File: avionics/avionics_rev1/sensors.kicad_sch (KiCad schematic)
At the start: 11 parts, among them U10 LSM6DSV32XTR, U8 LPS22DFTR, U9 ADXL375BCCZ-RL7

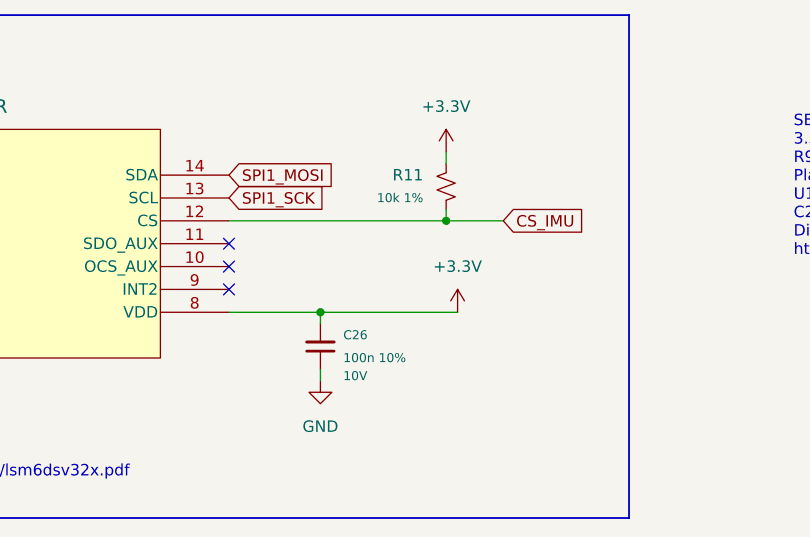
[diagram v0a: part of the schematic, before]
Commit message: cleaned up schematics after codex work
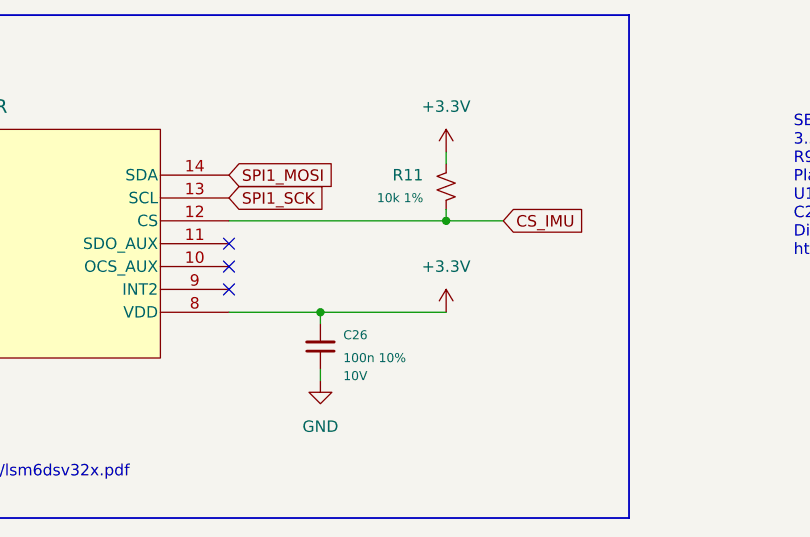
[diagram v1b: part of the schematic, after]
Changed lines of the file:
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@@
+	)
+	(junction
+		(at 124.46 119.38)
+		(diameter 0)
+		(color 0 0 0 0)
 	)
 	(junction
@@
 		(color 0 0 0 0)
 	)
-	(junction
-		(at 124.46 119.38)
-		(diameter 0)
-		(color 0 0 0 0)
-	)
 	(no_connect
 		(at 114.3 114.3)
@@
 	(wire
 		(pts
-			(xy 124.46 119.38) (xy 139.7 119.38)
+			(xy 124.46 119.38) (xy 138.43 119.38)
 		)
 		(stroke
@@
 	(symbol
 		(lib_id "power:+3.3V")
-		(at 139.7 119.38 0)
+		(at 138.43 119.38 0)
 		(unit 1)
 		(body_style 1)
@@
 		(fields_autoplaced yes)
 		(property "Reference" "#PWR047"
-			(at 139.7 123.19 0)
+			(at 138.43 123.19 0)
 			(hide yes)
 			(show_name no)
@@
 		)
 		(property "Value" "+3.3V"
-			(at 139.7 114.3 0)
+			(at 138.43 114.3 0)
 			(show_name no)
 			(do_not_autoplace no)
@@
 		)
 		(property "Footprint" ""
-			(at 139.7 119.38 0)
+			(at 138.43 119.38 0)
 			(hide yes)
 			(show_name no)
@@
 		)
 		(property "Datasheet" ""
-			(at 139.7 119.38 0)
+			(at 138.43 119.38 0)
 			(hide yes)
 			(show_name no)
@@
 		)
 		(property "Description" "Power symbol creates a global label with name \"+3.3V\""
-			(at 139.7 119.38 0)
-			(hide yes)
-			(show_name no)
+			(at 138.43 119.38 0)
+			(hide yes)
+			(show_name no)

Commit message: fixed ERC errors
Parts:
- C22, C23, C25, C26: value 100n 10% -> 100n; footprint Capacitor_SMD:C_0201_0603Metric -> Capacitor_SMD:C_0402_1005Metric; symbol Device:C_Small -> rocketry_library:GRM155R71A104KA01D; DigiKey (none) -> https://www.digikey.com/en/products/detail/murata-electroni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; MPN (none) -> GRM155R71A104KA01D
- C24: value 1u 10% -> 1u
- R10, R11, R9: value 10k 1% -> 10k; footprint Resistor_SMD:R_0201_0603Metric -> Resistor_SMD:R_0402_1005Metric; symbol Device:R_Small_US -> rocketry_library:RC0402FR-0710KL; DigiKey (none) -> https://www.digikey.com/en/products/detail/yageo/RC0402FR-0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; MPN (none) -> RC0402FR-0710KL; Voltage 25V -> 50V
- U10, U8: DigiKey (none) -> https://www.digikey.com/en/products/detail/stmicroelectroni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
- U9: DigiKey (none) -> https://www.digikey.com/en/products/detail/analog-devices-i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
